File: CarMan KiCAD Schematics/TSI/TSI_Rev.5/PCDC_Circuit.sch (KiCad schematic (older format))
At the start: 52 parts, among them IC1 TS431ILT, J30 GLV Hook-up Pin, K1 APAN3105, Q1 ZVP1320F, Q3 SI1302DL-T1-E3, U10 MC7805BDTRKG, U12 REF3033, U19 SN74HC00APWR, U21 MCP6004, U27 TLP293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

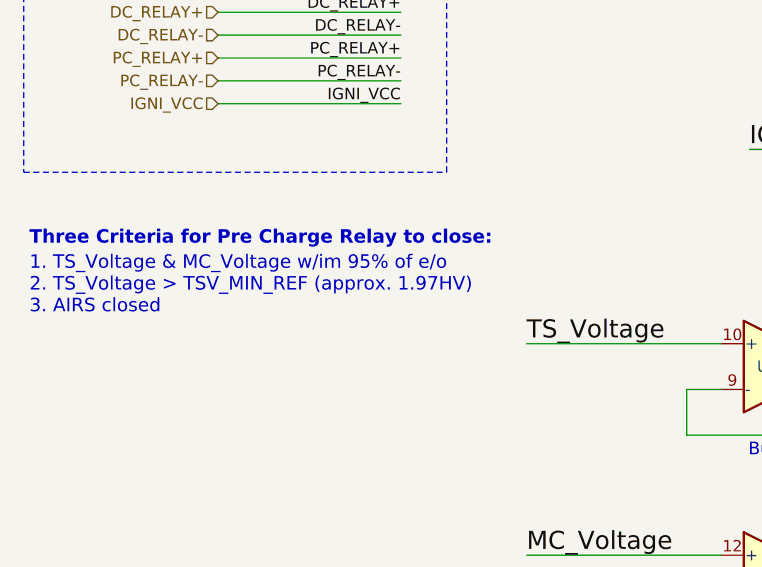
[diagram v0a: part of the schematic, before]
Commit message: Updated U19 footprint, changed to TSSOP-14, cross-referenced footprint with mouser product info footprint
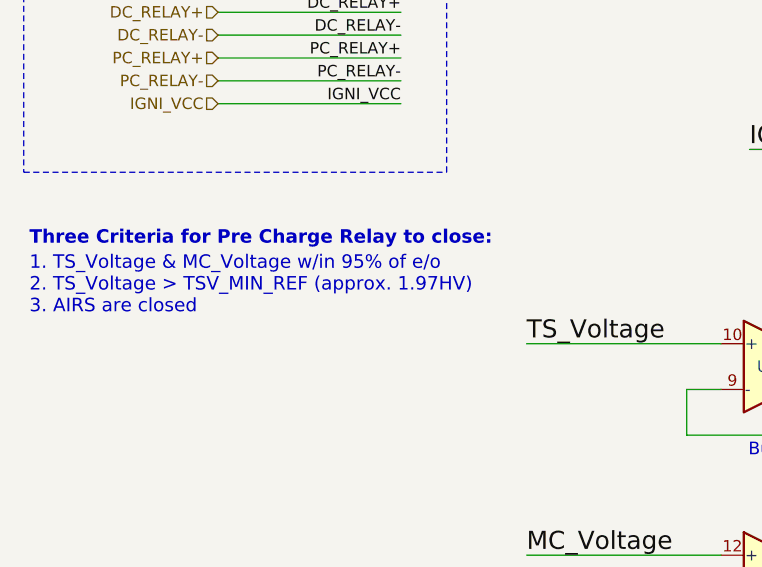
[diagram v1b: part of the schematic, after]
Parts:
- U19: footprint TSI_Rev_2021_Footprint_Lib:SOIC127P600X175-14N -> Package_SO:TSSOP-14_4.4x5mm_P0.65mm
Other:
- note added: "1. TS_Voltage & MC_Voltage w/in 95% of e/o\n2. TS_Voltage > TSV_MIN_REF (approx. 1.97HV)\n3. AIRS are closed"
- note removed: "1. TS_Voltage & MC_Voltage w/im 95% of e/o\n2. TS_Voltage > TSV_MIN_REF (approx. 1.97HV)\n3. AIRS closed"
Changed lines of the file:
@@
 $Descr A3 16535 11693
 encoding utf-8
-Sheet 2 6
+Sheet 5 6
 Title ""
 Date ""
@@
 F 0 "U19" H 7100 2950 50  0000 C CNN
 F 1 "SN74HC00APWR" H 7200 3150 50  0000 C CNN
-F 2 "TSI_Rev_2021_Footprint_Lib:SOIC127P600X175-14N" H 7100 2950 50  0001 C CNN
+F 2 "Package_SO:TSSOP-14_4.4x5mm_P0.65mm" H 7100 2950 50  0001 C CNN
 F 3 "http://www.ti.com/lit/gpn/sn74hc00" H 7100 2950 50  0001 C CNN
 F 4 "https://www.mouser.com/ProductDetail/Texas-Instruments/SN74HC00APWR?qs=6ZVwTuetbD5Of4SwrWZoMw%3D%3D" H 7100 2950 50  0001 C CNN "Mouser Link"
@@
 F 0 "U19" H 5400 4300 50  0000 C CNN
 F 1 "SN74HC00APWR" H 5400 4534 50  0000 C CNN
-F 2 "TSI_Rev_2021_Footprint_Lib:SOIC127P600X175-14N" H 5400 4300 50  0001 C CNN
+F 2 "Package_SO:TSSOP-14_4.4x5mm_P0.65mm" H 5400 4300 50  0001 C CNN
 F 3 "http://www.ti.com/lit/gpn/sn74hc00" H 5400 4300 50  0001 C CNN
 	2    5400 4300
@@
 F 0 "U19" H 8050 3050 50  0000 C CNN
 F 1 "SN74HC00APWR" H 8050 3250 50  0000 C CNN
-F 2 "TSI_Rev_2021_Footprint_Lib:SOIC127P600X175-14N" H 8050 3050 50  0001 C CNN
+F 2 "Package_SO:TSSOP-14_4.4x5mm_P0.65mm" H 8050 3050 50  0001 C CNN
 F 3 "http://www.ti.com/lit/gpn/sn74hc00" H 8050 3050 50  0001 C CNN
 	3    8050 3050
@@
 F 0 "U19" H 8050 3800 50  0000 C CNN
 F 1 "SN74HC00APWR" H 8050 3600 50  0000 C CNN
-F 2 "TSI_Rev_2021_Footprint_Lib:SOIC127P600X175-14N" H 8050 3800 50  0001 C CNN
+F 2 "Package_SO:TSSOP-14_4.4x5mm_P0.65mm" H 8050 3800 50  0001 C CNN
 F 3 "http://www.ti.com/lit/gpn/sn74hc00" H 8050 3800 50  0001 C CNN
 	4    8050 3800
@@
 F 0 "U19" V 7650 2100 50  0000 C CNN
 F 1 "SN74HC00APWR" V 7250 2100 50  0000 C CNN
-F 2 "TSI_Rev_2021_Footprint_Lib:SOIC127P600X175-14N" H 7500 2100 50  0001 C CNN
+F 2 "Package_SO:TSSOP-14_4.4x5mm_P0.65mm" H 7500 2100 50  0001 C CNN
 F 3 "http://www.ti.com/lit/gpn/sn74hc00" H 7500 2100 50  0001 C CNN
 	5    7500 2100
@@
 Text Notes 10975 2625 0    35   ~ 0
 Flyback\nDiode
-Text Notes 525  2525 0    59   ~ 0
-1. TS_Voltage & MC_Voltage w/im 95% of e/o\n2. TS_Voltage > TSV_MIN_REF (approx. 1.97HV)\n3. AIRS closed
 Text Notes 525  2225 0    59   ~ 12
 Three Criteria for Pre Charge Relay to close:
@@
 Text Notes 11475 8075 0    43   ~ 9
 TSV_MIN_REF Derivation:
+Text Notes 525  2525 0    59   ~ 0
+1. TS_Voltage & MC_Voltage w/in 95% of e/o\n2. TS_Voltage > TSV_MIN_REF (approx. 1.97HV)\n3. AIRS are closed
 $EndSCHEMATC

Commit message: redesigned Safety loop logic
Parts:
- removed R2: 95K, Resistor_SMD:R_0805_2012Metric_Pad1.15x1.40mm_HandSolder, symbol Device:R
- removed RV1: 3296W-1-103LF, Potentiometer_THT:Potentiometer_Bourns_3296W_Vertical, symbol Device:R_POT_TRIM
- removed U29: SN74LVC1G08DCKR, TSI_Rev_2021_Footprint_Lib:SOT65P210X110-5N, symbol TSI_Rev.5-rescue:SN74LVC1G08DCKR-SN74LVC1G08DCKR-Snap
- added C43, C5: 0.1u, Capacitor_SMD:C_0805_2012Metric_Pad1.15x1.40mm_HandSolder, symbol pspice:CAP
- added R72: 95K, Resistor_SMD:R_0805_2012Metric_Pad1.15x1.40mm_HandSolder, symbol Device:R
- added R75: 10K, Resistor_SMD:R_0805_2012Metric_Pad1.15x1.40mm_HandSolder, symbol Device:R
- added RV4: 3296W-1-103LF, Potentiometer_THT:Potentiometer_Bourns_3296W_Vertical, symbol Device:R_POT_TRIM
- added U41, U42: SN74HC00APWR, Package_SO:TSSOP-14_4.4x5mm_P0.65mm, symbol 74xx:74HC00
- TP4: value TSV_Ready_HV -> TSV_MIN
- TP5: value PC_Ready_HV -> MC_95%
- TP6: value PC_SL -> SLOOP_HV
- U19: Mouser Link (none) -> https://www.mouser.com/ProductDetail/Texas-Instruments/SN74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
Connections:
- net labels added: PC_Control, TSV_Ready
- net labels removed: PC_AND_SL_READY, TSV_Ready_HV
- wire segments 212 -> 268
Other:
- note added: "0\n"
- note added: "1"
- note added: "1. TS_Voltage & MC_Voltage w/in 95% of e/o\n2. TS_Voltage > TSV_MIN_REF (approx. 1.97HV)\n3. AIRS are closed (Safety_Loop_HV)"
- note added: "3-Input AND Gate"
- note added: "AND GATE"
- note added: "Ensures ~Q~ starts \nat 0V"
- note added: "INVERTER"
- note added: "OR GATE"
- note added: "SR Latching Logic\n"
- note added: "SR-LATCH"
- note added: "X"
- note added: "~Q\n"
- note added: "~R"
- note removed: "1. TS_Voltage & MC_Voltage w/in 95% of e/o\n2. TS_Voltage > TSV_MIN_REF (approx. 1.97HV)\n3. AIRS are closed"
- note removed: "5V"
- note removed: "AND Gate"
- note removed: "MC_Voltage > 95% of TS_Voltage"
- note removed: "N/A"
- note removed: "No Change"
- note removed: "SR Latch Logic\n"
- moved on the sheet: C1, C12, C2, C37, C38, D12, D13, D14, D6, D7, D8, IC1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

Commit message: Update
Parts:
- renumbered RV4 to RV1
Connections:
- net PC_Ready_HV renamed MC_95%
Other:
- note added: "1. TS_Voltage & MC_Voltage w/in 95% of e/o\n2. TS_Voltage > TSV_MIN_REF (approx. 1.97HV)\n3. AIRS are closed (Safety_Loop_HV = 5HV)"
- note added: "MC Voltage 95% Check"
- note removed: "1. TS_Voltage & MC_Voltage w/in 95% of e/o\n2. TS_Voltage > TSV_MIN_REF (approx. 1.97HV)\n3. AIRS are closed (Safety_Loop_HV)"
- moved on the sheet: U21D, U40B
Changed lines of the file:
@@
 TSV_MIN_REF Derivation:
 Text Notes 675  2650 0    79   ~ 0
-1. TS_Voltage & MC_Voltage w/in 95% of e/o\n2. TS_Voltage > TSV_MIN_REF (approx. 1.97HV)\n3. AIRS are closed (Safety_Loop_HV)
+1. TS_Voltage & MC_Voltage w/in 95% of e/o\n2. TS_Voltage > TSV_MIN_REF (approx. 1.97HV)\n3. AIRS are closed (Safety_Loop_HV = 5HV)
 Text Label 14600 6625 0    59   ~ 0
 PC_Control
@@
 Wire Wire Line
 	13550 6625 13550 6650
-Wire Wire Line
-	4550 5000 4450 5000
-Wire Wire Line
-	4550 5200 4550 5000
 Text Label 4900 5000 0    69   ~ 0
 TSV_Ready
 Text Label 4900 5200 0    69   ~ 0
-PC_Ready_HV
+MC_95%
 $Comp
 L Amplifier_Operational:MCP6004 U40
 U 2 1 616E5BE5
-P 4150 5000
-F 0 "U40" H 4150 5000 50  0000 C CNN
-F 1 "MCP6004" H 4350 4875 50  0000 C CNN
-F 2 "TSI_Rev_2021_Footprint_Lib:SOIC127P600X175-14N" H 4100 5100 50  0001 C CNN
-F 3 "http://www.ti.com/lit/gpn/sn74hc00" H 4200 5200 50  0001 C CNN
-	2    4150 5000
+P 4150 5200
+F 0 "U40" H 4150 5200 50  0000 C CNN
+F 1 "MCP6004" H 4350 5075 50  0000 C CNN
+F 2 "TSI_Rev_2021_Footprint_Lib:SOIC127P600X175-14N" H 4100 5300 50  0001 C CNN
+F 3 "http://www.ti.com/lit/gpn/sn74hc00" H 4200 5400 50  0001 C CNN
+	2    4150 5200
 	1    0    0    1
 $EndComp
@@
 	2075 3225 2750 3225
 Wire Wire Line
-	1800 5400 2600 5400
-Wire Wire Line
-	2600 5100 2600 5400
-Wire Wire Line
-	1800 5200 1800 5400
+	1800 5600 2600 5600
+Wire Wire Line
+	2600 5300 2600 5600
+Wire Wire Line
+	1800 5400 1800 5600
 Wire Wire Line
 	1100 4075 1950 4075
 Wire Wire Line
-	1100 5000 1950 5000
+	1100 5200 1950 5200
 Text Label 4050 4575 0    50   ~ 0
 IO_Ground
@@
 Text Notes 2300 4575 2    55   ~ 0
 Buffer\n
-Text Notes 2500 5500 2    55   ~ 0
+Text Notes 2500 5700 2    55   ~ 0
 Buffer\n
 Connection ~ 2750 4175
@@
 Wire Wire Line
 	2750 4175 2750 3925
-Text Label 1100 5000 0    79   ~ 0
+Text Label 1100 5200 0    79   ~ 0
 MC_Voltage
-Connection ~ 2600 5100
+Connection ~ 2600 5300
 Wire Wire Line
 	2600 4175 2750 4175
 Connection ~ 2600 4175
-$Comp
-L Device:R_POT_TRIM RV4
-U 1 1 616E5BC0
-P 2750 3775
-F 0 "RV4" H 2680 3821 50  0000 R CNN
-F 1 "3296W-1-103LF" H 2680 3730 50  0000 R CNN
-F 2 "Potentiometer_THT:Potentiometer_Bourns_3296W_Vertical" H 2750 3775 50  0001 C CNN
-F 3 "~" H 2750 3775 50  0001 C CNN
-	1    2750 3775
-	1    0    0    -1
-$EndComp
-Wire Wire Line
-	2600 5100 2550 5100
-Wire Wire Line
-	1950 5200 1800 5200
+Wire Wire Line
+	2600 5300 2550 5300
+Wire Wire Line
+	1950 5400 1800 5400
 Wire Wire Line
 	2600 4175 2550 4175
@@
 L Amplifier_Operational:MCP6004 U?
 U 4 1 616E5BAC
-P 2250 5100
+P 2250 5300
 AR Path="/5FC85F57/616E5BAC" Ref="U?"  Part="4"
 AR Path="/6196BF15/616E5BAC" Ref="U21"  Part="4"
-F 0 "U21" H 2200 5100 50  0000 C CNN
-F 1 "MCP6004" H 2400 4950 50  0000 C CNN
-F 2 "TSI_Rev_2021_Footprint_Lib:SOIC127P600X175-14N" H 2200 5200 50  0001 C CNN
-F 3 "http://www.ti.com/lit/gpn/sn74hc00" H 2300 5300 50  0001 C CNN
-	4    2250 5100
+F 0 "U21" H 2200 5300 50  0000 C CNN
+F 1 "MCP6004" H 2400 5150 50  0000 C CNN
+F 2 "TSI_Rev_2021_Footprint_Lib:SOIC127P600X175-14N" H 2200 5400 50  0001 C CNN
+F 3 "http://www.ti.com/lit/gpn/sn74hc00" H 2300 5500 50  0001 C CNN
+	4    2250 5300
 	1    0    0    -1
 $EndComp
@@
 	2750 4175 3850 4175
 Wire Wire Line
-	2600 5100 3850 5100
+	2600 5300 3850 5300
 Wire Wire Line
 	2900 3775 3075 3775
 Wire Wire Line
-	3075 3775 3075 4900
-Wire Wire Line
-	3075 4900 3850 4900
+	3075 5100 3850 5100
 Wire Wire Line
 	3300 4375 3850 4375
@@
 Wire Wire Line
 	4725 5000 5500 5000
-Wire Wire Line
-	4550 5200 5725 5200
 Wire Wire Line
 	4900 5425 5950 5425
@@
 Wire Wire Line
 	6250 12900 6800 12900
-Text Label 7100 15275 2    59   ~ 0
-PC_Ready_HV
 Wire Wire Line
 	4600 15850 5325 15850
@@
 Wire Notes Line
 	12075 5750 12075 6675
+$Comp
+L Device:R_POT_TRIM RV1
+U 1 1 616E5BC0
+P 2750 3775
+F 0 "RV1" H 2680 3821 50  0000 R CNN
+F 1 "3296W-1-103LF" H 2680 3730 50  0000 R CNN
+F 2 "Potentiometer_THT:Potentiometer_Bourns_3296W_Vertical" H 2750 3775 50  0001 C CNN
+F 3 "~" H 2750 3775 50  0001 C CNN
+	1    2750 3775
+	1    0    0    -1
+$EndComp
+Wire Wire Line
+	4450 5200 5725 5200
+Wire Wire Line
+	3075 3775 3075 5100
+Text Label 7100 15275 2    59   ~ 0
+MC_95%
+Wire Notes Line
+	4825 4750 4825 5475
+Wire Notes Line
+	3275 5475 4825 5475
+Wire Notes Line
+	3275 5475 3275 4750
+Wire Notes Line
+	3275 4750 4825 4750
+Text Notes 3525 4875 0    59   ~ 0
+MC Voltage 95% Check
 $EndSCHEMATC

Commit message: - Removed capacitors across R16, R53, R6 - Capacitive load was too much for 1.24HV Ref - Notes on Pre-charge circuit & Throttle Plausibility - Cooling, Relays & Voltage Refs
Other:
- note added: "95% of \nVoltage"
- note added: "Let's say 45HV is the minimum TSV Voltage to operate circuit,\n45HV * 1/61 voltage div. = 0.74HV\n0.74HV + 1.24HV_Ref bias signal = 1.97HV\n1.97HV -> TSV_MIN_REF\n"
- note added: "NAND Package Power Supplies"
- note added: "PRE-CHARGE LOGIC CIRCUIT"
- note added: "VOLTAGE REFERENCES & REGULATORS (HIGH VOLTAGE)"
- note removed: "45HV * 1/61 voltage div. = 0.74HV\n0.74HV + 1.24HV_Ref bias signal = 1.97HV\n1.97HV -> TSV_MIN_REF\n"
- note removed: "95% of Voltage"
- note removed: "NAND Package \nPower Supplies"
- note removed: "VOLTAGE REFERENCES & REGULATORS\n(HIGH VOLTAGE)"
- moved on the sheet: C1, C12, C37, C43, C5, IC1, R101, R46, R72, RV1, RV3, U10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
